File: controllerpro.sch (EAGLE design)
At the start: 10 parts

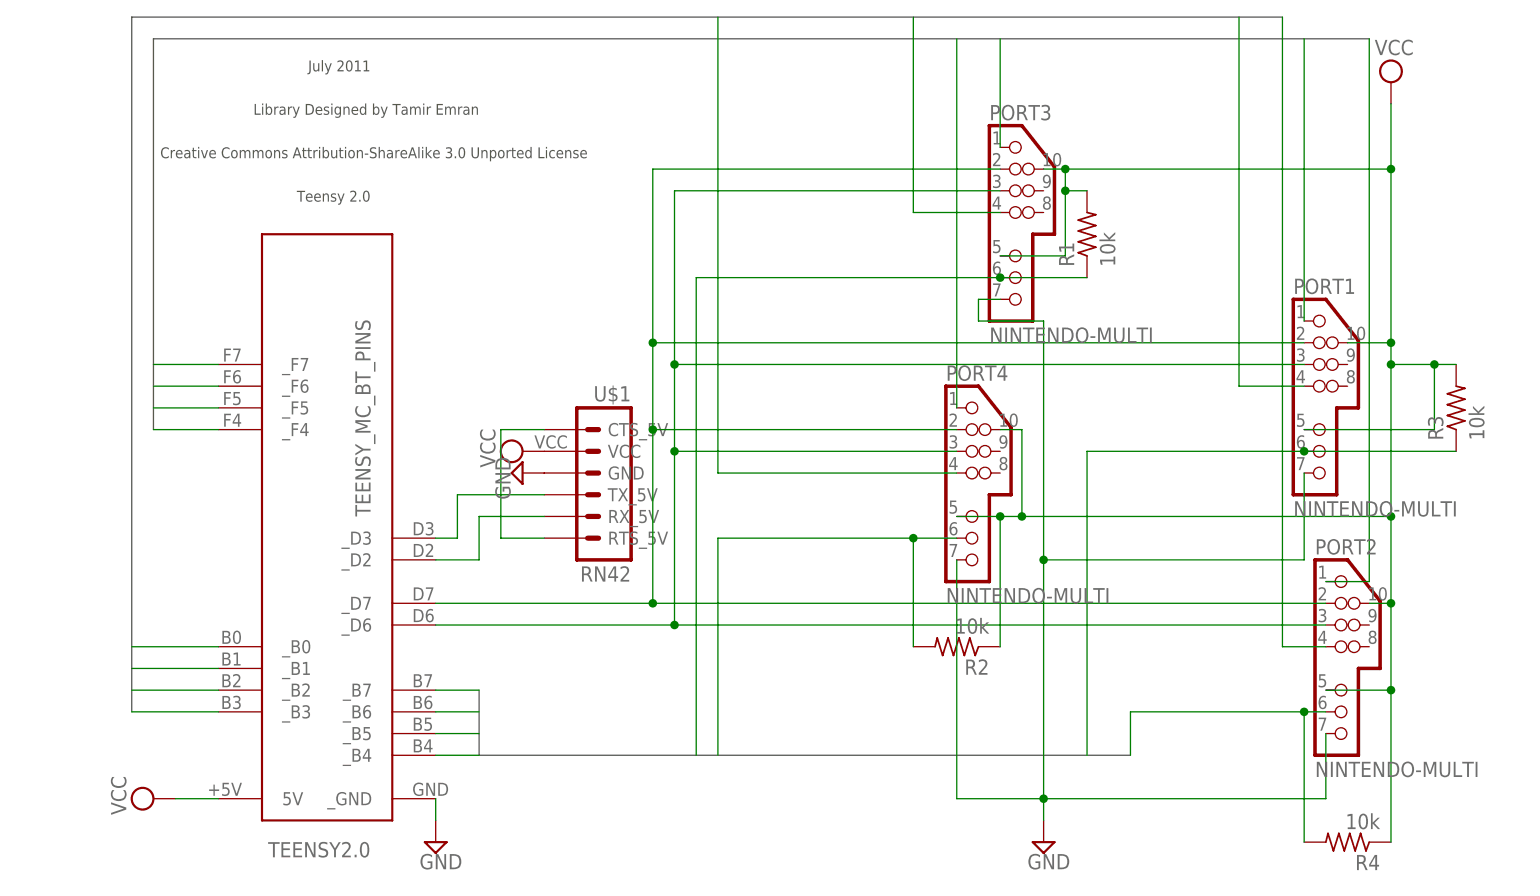
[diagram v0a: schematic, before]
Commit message: Remove pull-up resistors for N64
Not necessary any more now that Teensy is at 3.3v
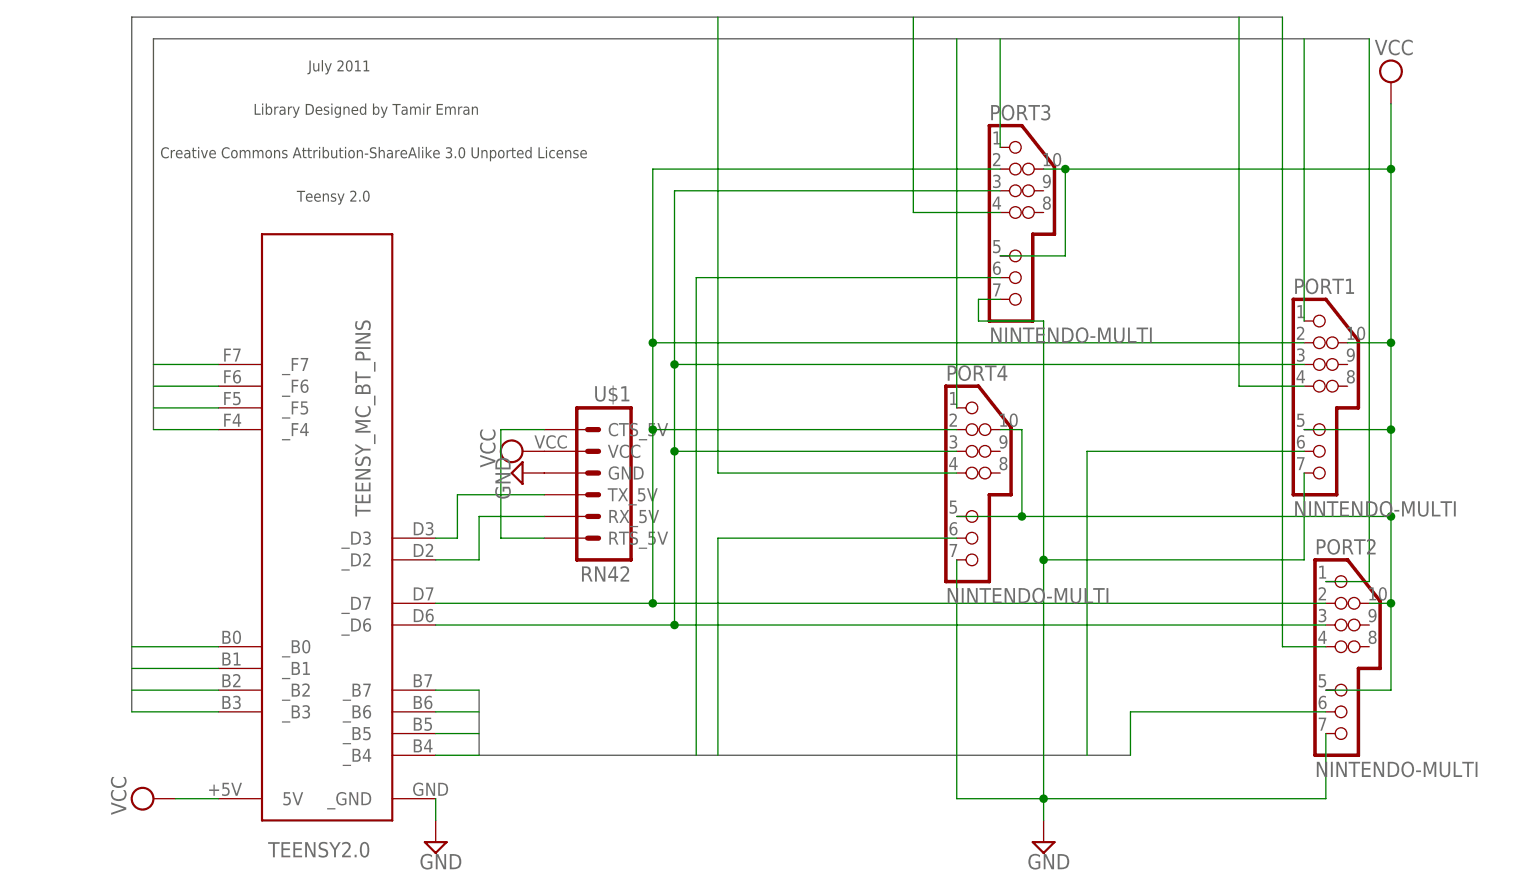
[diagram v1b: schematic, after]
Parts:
- removed R1, R2, R3, R4: 10k, rcl:R-US_R0603
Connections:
- net 3VDATA0: no longer R1.1
- net 3VDATA1: no longer R2.2
- net 3VDATA2: no longer R3.1
- net 3VDATA3: no longer R4.2
- net VCC: no longer R1.2, R2.1, R3.2, R4.1
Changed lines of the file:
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@@
 <part name="TEENSY2.0" library="custom" deviceset="TEENSY_MC_BT_PINS" device=""/>
 <part name="SUPPLY6" library="supply2" deviceset="GND" device=""/>
-<part name="R4" library="rcl" deviceset="R-US_" device="R0603" value="10k"/>
-<part name="R2" library="rcl" deviceset="R-US_" device="R0603" value="10k"/>
-<part name="R1" library="rcl" deviceset="R-US_" device="R0603" value="10k"/>
-<part name="R3" library="rcl" deviceset="R-US_" device="R0603" value="10k"/>
 <part name="U$1" library="SparkFun-Boards" deviceset="RN42" device=""/>
 <part name="SUPPLY4" library="supply2" deviceset="GND" device=""/>
@@
 <instance part="TEENSY2.0" gate="G$1" x="40.64" y="53.34" rot="R180"/>
 <instance part="SUPPLY6" gate="GND" x="53.34" y="15.24"/>
-<instance part="R4" gate="G$1" x="160.02" y="15.24" rot="R180"/>
-<instance part="R2" gate="G$1" x="114.3" y="38.1" rot="R180"/>
-<instance part="R1" gate="G$1" x="129.54" y="86.36" rot="R90"/>
-<instance part="R3" gate="G$1" x="172.72" y="66.04" rot="R90"/>
 <instance part="U$1" gate="G$1" x="71.12" y="58.42" rot="MR0"/>
 <instance part="SUPPLY4" gate="GND" x="63.5" y="58.42" rot="R270"/>
@@
 <wire x1="165.1" y1="43.18" x2="165.1" y2="53.34" width="0.1524" layer="91"/>
 <pinref part="PORT1" gate="G$1" pin="10"/>
-<wire x1="165.1" y1="53.34" x2="165.1" y2="71.12" width="0.1524" layer="91"/>
-<wire x1="165.1" y1="71.12" x2="165.1" y2="73.66" width="0.1524" layer="91"/>
+<wire x1="165.1" y1="53.34" x2="165.1" y2="63.5" width="0.1524" layer="91"/>
+<wire x1="165.1" y1="63.5" x2="165.1" y2="73.66" width="0.1524" layer="91"/>
 <wire x1="165.1" y1="73.66" x2="165.1" y2="93.98" width="0.1524" layer="91"/>
 <wire x1="160.02" y1="73.66" x2="165.1" y2="73.66" width="0.1524" layer="91"/>
@@
 <junction x="165.1" y="93.98"/>
 <pinref part="PORT4" gate="G$1" pin="5"/>
-<wire x1="119.38" y1="53.34" x2="114.3" y2="53.34" width="0.1524" layer="91"/>
-<pinref part="R2" gate="G$1" pin="1"/>
-<wire x1="119.38" y1="38.1" x2="119.38" y2="53.34" width="0.1524" layer="91"/>
-<junction x="119.38" y="53.34"/>
-<wire x1="121.92" y1="53.34" x2="119.38" y2="53.34" width="0.1524" layer="91"/>
+<wire x1="121.92" y1="53.34" x2="114.3" y2="53.34" width="0.1524" layer="91"/>
 <pinref part="PORT3" gate="G$1" pin="5"/>
 <wire x1="119.38" y1="83.82" x2="127" y2="83.82" width="0.1524" layer="91"/>
-<wire x1="127" y1="91.44" x2="127" y2="83.82" width="0.1524" layer="91"/>
-<pinref part="R1" gate="G$1" pin="2"/>
-<wire x1="129.54" y1="91.44" x2="127" y2="91.44" width="0.1524" layer="91"/>
-<wire x1="127" y1="91.44" x2="127" y2="93.98" width="0.1524" layer="91"/>
+<wire x1="127" y1="93.98" x2="127" y2="83.82" width="0.1524" layer="91"/>
 <junction x="127" y="93.98"/>
-<junction x="127" y="91.44"/>
-<pinref part="PORT1" gate="G$1" pin="5"/>
-<pinref part="R3" gate="G$1" pin="2"/>
-<wire x1="172.72" y1="71.12" x2="170.18" y2="71.12" width="0.1524" layer="91"/>
-<wire x1="170.18" y1="71.12" x2="170.18" y2="63.5" width="0.1524" layer="91"/>
-<wire x1="170.18" y1="63.5" x2="154.94" y2="63.5" width="0.1524" layer="91"/>
-<junction x="170.18" y="71.12"/>
-<wire x1="170.18" y1="71.12" x2="165.1" y2="71.12" width="0.1524" layer="91"/>
-<junction x="165.1" y="71.12"/>
 <junction x="121.92" y="53.34"/>
-<pinref part="R4" gate="G$1" pin="1"/>
 <pinref part="PORT2" gate="G$1" pin="5"/>
 <wire x1="157.48" y1="33.02" x2="165.1" y2="33.02" width="0.1524" layer="91"/>
-<wire x1="165.1" y1="33.02" x2="165.1" y2="15.24" width="0.1524" layer="91"/>
 <wire x1="165.1" y1="43.18" x2="165.1" y2="33.02" width="0.1524" layer="91"/>
-<junction x="165.1" y="33.02"/>
 <junction x="165.1" y="43.18"/>
+<pinref part="PORT1" gate="G$1" pin="5"/>
+<junction x="165.1" y="63.5"/>
+<wire x1="165.1" y1="63.5" x2="154.94" y2="63.5" width="0.1524" layer="91"/>
 </segment>
 <segment>
@@
 <wire x1="83.82" y1="25.4" x2="83.82" y2="81.28" width="0.1524" layer="91"/>
 <pinref part="PORT3" gate="G$1" pin="6"/>
-<pinref part="R1" gate="G$1" pin="1"/>
-<wire x1="119.38" y1="81.28" x2="129.54" y2="81.28" width="0.1524" layer="91"/>
-<junction x="119.38" y="81.28"/>
 <wire x1="119.38" y1="81.28" x2="83.82" y2="81.28" width="0.1524" layer="91"/>
 </segment>
@@
 <wire x1="86.36" y1="25.4" x2="86.36" y2="50.8" width="0.1524" layer="91"/>
 <pinref part="PORT4" gate="G$1" pin="6"/>
-<wire x1="109.22" y1="50.8" x2="114.3" y2="50.8" width="0.1524" layer="91"/>
-<pinref part="R2" gate="G$1" pin="2"/>
-<wire x1="109.22" y1="38.1" x2="109.22" y2="50.8" width="0.1524" layer="91"/>
-<wire x1="109.22" y1="50.8" x2="86.36" y2="50.8" width="0.1524" layer="91"/>
-<junction x="109.22" y="50.8"/>
+<wire x1="114.3" y1="50.8" x2="86.36" y2="50.8" width="0.1524" layer="91"/>
 </segment>
 <segment>
@@
 <pinref part="PORT1" gate="G$1" pin="6"/>
 <wire x1="129.54" y1="60.96" x2="129.54" y2="25.4" width="0.1524" layer="91"/>
-<pinref part="R3" gate="G$1" pin="1"/>
-<wire x1="154.94" y1="60.96" x2="172.72" y2="60.96" width="0.1524" layer="91"/>
-<junction x="154.94" y="60.96"/>
 <wire x1="154.94" y1="60.96" x2="129.54" y2="60.96" width="0.1524" layer="91"/>
 </segment>
@@
 <segment>
 <pinref part="PORT2" gate="G$1" pin="6"/>
-<pinref part="R4" gate="G$1" pin="2"/>
-<wire x1="154.94" y1="30.48" x2="157.48" y2="30.48" width="0.1524" layer="91"/>
-<wire x1="154.94" y1="15.24" x2="154.94" y2="30.48" width="0.1524" layer="91"/>
-<wire x1="154.94" y1="30.48" x2="134.62" y2="30.48" width="0.1524" layer="91"/>
+<wire x1="157.48" y1="30.48" x2="134.62" y2="30.48" width="0.1524" layer="91"/>
 <wire x1="134.62" y1="30.48" x2="134.62" y2="25.4" width="0.1524" layer="91"/>
-<junction x="154.94" y="30.48"/>
-</segment>
-<segment>
+</segment>
+<segment>

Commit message: Update RN42 and move to our custom lib
Get the footprint/silkscreen on the right side and things
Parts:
- U$1: device SparkFun-Boards:RN42 -> custom:RN42
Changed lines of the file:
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@@
 <part name="TEENSY2.0" library="custom" deviceset="TEENSY_MC_BT_PINS" device=""/>
 <part name="SUPPLY6" library="supply2" deviceset="GND" device=""/>
-<part name="U$1" library="SparkFun-Boards" deviceset="RN42" device=""/>
+<part name="U$1" library="custom" deviceset="RN42" device=""/>
 <part name="SUPPLY4" library="supply2" deviceset="GND" device=""/>
 <part name="SUPPLY5" library="supply2" deviceset="VCC" device=""/>
